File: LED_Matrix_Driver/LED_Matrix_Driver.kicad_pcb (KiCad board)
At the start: 2 copper layers, 64 parts, among them J1 5V_DC, J2 I2C Bus, J3 LED Anode Rows, J4 Columns 24-31 LED Cathodes, J5 Columns 16-23 LED Cathodes, J6 Columns 8-15 LED Cathodes, J7 Columns 0-7 LED Cathodes, U1 ATmega8-16PU, U2 74HC238, U3 MIC2981, U4 HEF4794B, U5 HEF4794B, U6 HEF4794B, U7 HEF4794B, Y1 16MHz

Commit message: Big Commit:
- Hardware files are complete
    - Final hardware iteration until further notice.
- Generated new firmware project with Platform.io in VSCode
    - Will use git more with this
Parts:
- removed C5, C6, C7: 0.1uF, Capacitor_THT:C_Axial_L3.8mm_D2.6mm_P7.50mm_Horizontal
- removed J7: Columns 0-7 LED Cathodes, TerminalBlock_Phoenix:TerminalBlock_Phoenix_MKDS-1,5-8-5.08_1x08_P5.08mm_Horizontal
- removed Y1: 16MHz, Crystal:Crystal_HC49-U_Vertical
- added R43: 200, Resistor_THT:R_Axial_DIN0204_L3.6mm_D1.6mm_P7.62mm_Horizontal, F.Cu at (262.0, 25.4)
- added R44: 200, Resistor_THT:R_Axial_DIN0204_L3.6mm_D1.6mm_P7.62mm_Horizontal, F.Cu at (266.7, 25.4)
- added R45: 200, Resistor_THT:R_Axial_DIN0204_L3.6mm_D1.6mm_P7.62mm_Horizontal, F.Cu at (271.8, 25.4)
- added R46: 200, Resistor_THT:R_Axial_DIN0204_L3.6mm_D1.6mm_P7.62mm_Horizontal, F.Cu at (276.9, 25.4)
- added R47: 200, Resistor_THT:R_Axial_DIN0204_L3.6mm_D1.6mm_P7.62mm_Horizontal, F.Cu at (281.9, 25.4)
- added U8: HEF4794B, Package_DIP:DIP-16_W7.62mm_Socket, F.Cu at (262.9, 47.0)
- C1, C2: value 22pF -> 0.1uF
- C3, C4: moved to F.Cu
- J1: value 5V_DC -> Screw_Terminal_01x02; footprint Connector_BarrelJack:BarrelJack_Horizontal -> TerminalBlock_4Ucon:TerminalBlock_4Ucon_1x02_P3.50mm_Horizontal
- J2: value I2C Bus -> LED Anode Rows; footprint TerminalBlock_Phoenix:TerminalBlock_Phoenix_MKDS-1,5-2-5.08_1x02_P5.08mm_Horizontal -> TerminalBlock_Phoenix:TerminalBlock_Phoenix_MKDS-1,5-8-5.08_1x08_P5.08mm_Horizontal
- J3: value LED Anode Rows -> Columns 24-31 LED Cathodes
- J4: value Columns 24-31 LED Cathodes -> Columns 16-23 LED Cathodes
- J5: value Columns 16-23 LED Cathodes -> Columns 8-15 LED Cathodes
- J6: value Columns 8-15 LED Cathodes -> Columns 0-7 LED Cathodes
- R1, R2: value 10k -> 1M
- R11, R12, R13, R14, R15: value 200 -> 3k3
- R3, R4, R5, R6, R7: value 3k3 -> 1M
- U1: value ATmega8-16PU -> ESP32-DEVKITC-32E; footprint Package_DIP:DIP-28_W7.62mm_Socket -> Arduino:ESP32-DevkitC
- U2: value 74HC238 -> 74HCT244; footprint Package_DIP:DIP-16_W7.62mm_Socket -> Package_DIP:DIP-20_W7.62mm_Socket
- U4: value HEF4794B -> 74HC238
- moved R42 195.4 mm to (256.5, 25.4), turned to 270 degrees
- moved R41 187.5 mm to (251.5, 25.4), turned to 270 degrees
- moved R40 179.8 mm to (246.4, 25.4), turned to 270 degrees
- moved R39 171.5 mm to (240.0, 25.4), turned to 270 degrees
- moved J4 170.7 mm to (162.6, 17.8), turned to 0 degrees
- moved R16 168.8 mm to (120.7, 25.4), turned to 270 degrees
- moved R38 164.5 mm to (234.9, 25.4), turned to 270 degrees
- moved R17 161.9 mm to (125.7, 25.4), turned to 270 degrees
- moved R37 157.7 mm to (229.9, 25.4), turned to 270 degrees
- moved R18 155.3 mm to (130.8, 25.4), turned to 270 degrees
- moved J6 152.2 mm to (246.4, 17.8), turned to 0 degrees
- moved R36 151.4 mm to (224.8, 25.4), turned to 270 degrees
- moved R19 148.4 mm to (135.9, 25.4), turned to 270 degrees
- moved J1 146.1 mm to (121.9, 90.8), turned to 90 degrees
- moved R35 145.5 mm to (219.7, 25.4), turned to 270 degrees
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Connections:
- C1 pad 1: Net-(C1-Pad1) -> +5V
- C2 pad 1: Net-(C2-Pad1) -> +5V
- J1 pad 1: Earth -> +5V
- J1 pad 2: +5V -> Earth
- R1 pad 1: Net-(J2-Pad1) -> Net-(R1-Pad1)
- R1 pad 2: +5V -> Earth
- R11 pad 1: Net-(J4-Pad1) -> Net-(R11-Pad1)
- R12 pad 1: Net-(J4-Pad2) -> Net-(R12-Pad1)
- R13 pad 1: Net-(J4-Pad3) -> Net-(R13-Pad1)
- R14 pad 1: Net-(J4-Pad4) -> Net-(R14-Pad1)
- R15 pad 1: Net-(J4-Pad5) -> Net-(R15-Pad1)
- R16 pad 1: Net-(J4-Pad6) -> Net-(J3-Pad1)
- R17 pad 1: Net-(J4-Pad7) -> Net-(J3-Pad2)
- R18 pad 1: Net-(J4-Pad8) -> Net-(J3-Pad3)
- R19 pad 1: Net-(J5-Pad1) -> Net-(J3-Pad4)
- R2 pad 1: Net-(J2-Pad2) -> Net-(R2-Pad1)
- R2 pad 2: +5V -> Earth
- R20 pad 1: Net-(J5-Pad2) -> Net-(J3-Pad5)
- R21 pad 1: Net-(J5-Pad3) -> Net-(J3-Pad6)
- R22 pad 1: Net-(J5-Pad4) -> Net-(J3-Pad7)
- R23 pad 1: Net-(J5-Pad5) -> Net-(J3-Pad8)
- R24 pad 1: Net-(J5-Pad6) -> Net-(J4-Pad1)
- R25 pad 1: Net-(J5-Pad7) -> Net-(J4-Pad2)
- R26 pad 1: Net-(J5-Pad8) -> Net-(J4-Pad3)
- R27 pad 1: Net-(J6-Pad1) -> Net-(J4-Pad4)
- R28 pad 1: Net-(J6-Pad2) -> Net-(J4-Pad5)
- R29 pad 1: Net-(J6-Pad3) -> Net-(J4-Pad6)
- R3 pad 2: Net-(R3-Pad2) -> Earth
- R30 pad 1: Net-(J6-Pad4) -> Net-(J4-Pad7)
- R31 pad 1: Net-(J6-Pad5) -> Net-(J4-Pad8)
- R32 pad 1: Net-(J6-Pad6) -> Net-(J5-Pad1)
- R33 pad 1: Net-(J6-Pad7) -> Net-(J5-Pad2)
- R34 pad 1: Net-(J6-Pad8) -> Net-(J5-Pad3)
- R35 pad 1: Net-(J7-Pad1) -> Net-(J5-Pad4)
- R36 pad 1: Net-(J7-Pad2) -> Net-(J5-Pad5)
- R37 pad 1: Net-(J7-Pad3) -> Net-(J5-Pad6)
- R38 pad 1: Net-(J7-Pad4) -> Net-(J5-Pad7)
- R39 pad 1: Net-(J7-Pad5) -> Net-(J5-Pad8)
- R4 pad 2: Net-(R4-Pad2) -> Earth
- R40 pad 1: Net-(J7-Pad6) -> Net-(J6-Pad1)
- R41 pad 1: Net-(J7-Pad7) -> Net-(J6-Pad2)
- R42 pad 1: Net-(J7-Pad8) -> Net-(J6-Pad3)
- R5 pad 2: Net-(R5-Pad2) -> Earth
- R6 pad 2: Net-(R6-Pad2) -> Earth
- R7 pad 2: Net-(R7-Pad2) -> Earth
- U1 pad 10: Net-(C2-Pad1) -> Net-(U1-Pad10)
- U1 pad 12: Net-(U1-Pad12) -> Net-(R5-Pad1)
- U1 pad 13: Net-(U1-Pad13) -> Net-(R7-Pad1)
- U1 pad 14: Net-(U1-Pad14) -> Earth
- U1 pad 15: Net-(U1-Pad15) -> Net-(R6-Pad1)
- U1 pad 19: Net-(U1-Pad19) -> +5V
- U1 pad 20: +5V -> Net-(U1-Pad20)
- U1 pad 22: Earth -> Net-(U1-Pad22)
- U1 pad 23: Net-(U1-Pad23) -> Net-(R4-Pad1)
- U1 pad 27: Net-(J2-Pad1) -> Net-(R3-Pad1)
- U1 pad 28: Net-(J2-Pad2) -> Net-(R2-Pad1)
- U1 pad 7: +5V -> Net-(U1-Pad7)
- U1 pad 8: Earth -> Net-(U1-Pad8)
- U1 pad 9: Net-(C1-Pad1) -> Net-(U1-Pad9)
- U2 pad 1: Net-(U1-Pad11) -> Earth
- U2 pad 10: Net-(R5-Pad2) -> Earth
- U2 pad 11: Net-(R6-Pad2) -> Net-(U2-Pad11)
- U2 pad 12: Net-(R7-Pad2) -> Net-(U2-Pad12)
- U2 pad 13: Net-(R8-Pad2) -> Net-(R1-Pad1)
- U2 pad 14: Net-(R9-Pad2) -> Net-(U2-Pad14)
- U2 pad 15: Net-(R10-Pad2) -> Net-(R2-Pad1)
- U2 pad 16: +5V -> Net-(U2-Pad16)
- U2 pad 2: Net-(U1-Pad12) -> Net-(R7-Pad1)
- U2 pad 3: Net-(U1-Pad13) -> Net-(U2-Pad3)
- U2 pad 4: Earth -> Net-(R6-Pad1)
- U2 pad 5: Earth -> Net-(U2-Pad5)
- U2 pad 6: +5V -> Net-(R5-Pad1)
- U2 pad 7: Net-(R3-Pad2) -> Net-(U2-Pad7)
- U2 pad 8: Earth -> Net-(R4-Pad1)
- U2 pad 9: Net-(R4-Pad2) -> Net-(U2-Pad9)
- U3 pad 1: Net-(R10-Pad1) -> Net-(R15-Pad1)
- U3 pad 11: Net-(J3-Pad8) -> Net-(J2-Pad8)
- U3 pad 12: Net-(J3-Pad7) -> Net-(J2-Pad7)
- U3 pad 13: Net-(J3-Pad6) -> Net-(J2-Pad6)
- U3 pad 14: Net-(J3-Pad5) -> Net-(J2-Pad5)
- U3 pad 15: Net-(J3-Pad4) -> Net-(J2-Pad4)
- U3 pad 16: Net-(J3-Pad3) -> Net-(J2-Pad3)
- U3 pad 17: Net-(J3-Pad2) -> Net-(J2-Pad2)
- U3 pad 18: Net-(J3-Pad1) -> Net-(J2-Pad1)
- U3 pad 2: Net-(R9-Pad1) -> Net-(R14-Pad1)
- U3 pad 3: Net-(R8-Pad1) -> Net-(R13-Pad1)
- U3 pad 4: Net-(R7-Pad1) -> Net-(R12-Pad1)
- U3 pad 5: Net-(R6-Pad1) -> Net-(R11-Pad1)
- U3 pad 6: Net-(R5-Pad1) -> Net-(R10-Pad1)
- U3 pad 7: Net-(R4-Pad1) -> Net-(R9-Pad1)
- U3 pad 8: Net-(R3-Pad1) -> Net-(R8-Pad1)
- U4 pad 1: Net-(U1-Pad14) -> Net-(U2-Pad3)
- U4 pad 10: Net-(U4-Pad10) -> Net-(R10-Pad2)
- U4 pad 11: Net-(R18-Pad2) -> Net-(R11-Pad2)
- U4 pad 12: Net-(R17-Pad2) -> Net-(R12-Pad2)
- U4 pad 13: Net-(R16-Pad2) -> Net-(R13-Pad2)
- U4 pad 14: Net-(R15-Pad2) -> Net-(R14-Pad2)
- U4 pad 15: Net-(U1-Pad17) -> Net-(R15-Pad2)
- U4 pad 2: Net-(U1-Pad15) -> Net-(U2-Pad5)
- U4 pad 3: Net-(U1-Pad16) -> Net-(U2-Pad7)
- U4 pad 4: Net-(R11-Pad2) -> Earth
- U4 pad 5: Net-(R12-Pad2) -> Earth
- U4 pad 6: Net-(R13-Pad2) -> +5V
- U4 pad 7: Net-(R14-Pad2) -> Net-(R8-Pad2)
- U4 pad 9: Net-(U4-Pad9) -> Net-(R9-Pad2)
- U5 pad 1: Net-(U1-Pad14) -> Net-(U2-Pad18)
- U5 pad 11: Net-(R26-Pad2) -> Net-(R23-Pad2)
- U5 pad 12: Net-(R25-Pad2) -> Net-(R22-Pad2)
- U5 pad 13: Net-(R24-Pad2) -> Net-(R21-Pad2)
- U5 pad 14: Net-(R23-Pad2) -> Net-(R20-Pad2)
- U5 pad 15: Net-(U1-Pad17) -> Net-(U2-Pad12)
- U5 pad 2: Net-(U4-Pad9) -> Net-(U2-Pad16)
- U5 pad 3: Net-(U1-Pad16) -> Net-(U2-Pad14)
- U5 pad 4: Net-(R19-Pad2) -> Net-(R16-Pad2)
- U5 pad 5: Net-(R20-Pad2) -> Net-(R17-Pad2)
- U5 pad 6: Net-(R21-Pad2) -> Net-(R18-Pad2)
- U5 pad 7: Net-(R22-Pad2) -> Net-(R19-Pad2)
- U6 pad 1: Net-(U1-Pad14) -> Net-(U2-Pad18)
- U6 pad 11: Net-(R34-Pad2) -> Net-(R31-Pad2)
- U6 pad 12: Net-(R33-Pad2) -> Net-(R30-Pad2)
- U6 pad 13: Net-(R32-Pad2) -> Net-(R29-Pad2)
- U6 pad 14: Net-(R31-Pad2) -> Net-(R28-Pad2)
- U6 pad 15: Net-(U1-Pad17) -> Net-(U2-Pad12)
- U6 pad 3: Net-(U1-Pad16) -> Net-(U2-Pad14)
- U6 pad 4: Net-(R27-Pad2) -> Net-(R24-Pad2)
- U6 pad 5: Net-(R28-Pad2) -> Net-(R25-Pad2)
- U6 pad 6: Net-(R29-Pad2) -> Net-(R26-Pad2)
- U6 pad 7: Net-(R30-Pad2) -> Net-(R27-Pad2)
- U7 pad 1: Net-(U1-Pad14) -> Net-(U2-Pad18)
- U7 pad 11: Net-(R42-Pad2) -> Net-(R39-Pad2)
- U7 pad 12: Net-(R41-Pad2) -> Net-(R38-Pad2)
- U7 pad 13: Net-(R40-Pad2) -> Net-(R37-Pad2)
- U7 pad 14: Net-(R39-Pad2) -> Net-(R36-Pad2)
- U7 pad 15: Net-(U1-Pad17) -> Net-(U2-Pad12)
- U7 pad 3: Net-(U1-Pad16) -> Net-(U2-Pad14)
- U7 pad 4: Net-(R35-Pad2) -> Net-(R32-Pad2)
- U7 pad 5: Net-(R36-Pad2) -> Net-(R33-Pad2)
- U7 pad 6: Net-(R37-Pad2) -> Net-(R34-Pad2)
- U7 pad 7: Net-(R38-Pad2) -> Net-(R35-Pad2)
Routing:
- net Net-(U1-Pad17): track 163.9 -> 0.00 mm
- net Net-(U1-Pad14): track 161.5 -> 0.00 mm
- net Net-(U2-Pad18): track 0.00 -> 159.6 mm, vias 0 -> 1
- net Net-(U2-Pad12): track 0.00 -> 158.8 mm, vias 0 -> 1
- net Net-(U1-Pad16): track 153.0 -> 0.00 mm, vias 4 -> 0
- net Net-(U2-Pad14): track 0.00 -> 147.0 mm, vias 0 -> 3
- net Net-(R1-Pad1): track 0.00 -> 80.8 mm
- net Net-(U2-Pad16): track 0.00 -> 76.2 mm, vias 0 -> 1
- net Net-(R2-Pad1): track 0.00 -> 70.3 mm
- net Net-(J2-Pad2): track 75.3 -> 9.42 mm
- net Net-(J2-Pad1): track 74.9 -> 9.42 mm
- net Net-(R5-Pad1): track 7.62 -> 66.3 mm
- net Net-(R4-Pad1): track 7.62 -> 63.4 mm
- net Net-(R3-Pad1): track 7.62 -> 62.3 mm
- net Net-(U1-Pad15): track 51.8 -> 0.00 mm, vias 1 -> 0
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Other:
- board outline added: 168.3 x 82.6 mm
- board text added: "5V"
- board text added: "8x32 LED Matrix Driver"
- board text added: "BACK OF BOARD"
- board text added: "Copyright (C) Matt Bowen 2023"
- board text added: "Designed by Matt Bowen"

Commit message: Made some minor tweaks to the PCB layout. Will not physically implement them until later date.
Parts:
- removed C1: 0.1uF, Capacitor_THT:C_Axial_L3.8mm_D2.6mm_P7.50mm_Horizontal
- moved U1 58.4 mm to (179.7, 68.6), turned to 270 degrees
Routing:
- net Net-(R6-Pad1): track 51.5 -> 74.1 mm
- net Net-(R4-Pad1): track 63.4 -> 81.8 mm
- net Net-(R1-Pad1): track 80.8 -> 65.9 mm
- net Net-(R7-Pad1): track 51.5 -> 60.8 mm
- net Net-(R2-Pad1): track 70.3 -> 65.9 mm
- net Net-(R3-Pad1): track 62.3 -> 65.2 mm
- net Net-(R5-Pad1): track 66.3 -> 68.4 mm
- net +5V: track 476.7 -> 475.1 mm
- net Earth: vias 20 -> 37

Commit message: Created a new PCB layout for LEDMatrixDriver board
- More compact
- Removed unused capacitors
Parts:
- removed C2, C3, C4: 0.1uF, Capacitor_THT:C_Axial_L3.8mm_D2.6mm_P7.50mm_Horizontal
- R1, R2, R3, R4, R5, R6, R7: footprint Resistor_THT:R_Axial_DIN0204_L3.6mm_D1.6mm_P7.62mm_Horizontal -> Resistor_THT:R_Axial_DIN0207_L6.3mm_D2.5mm_P10.16mm_Horizontal; moved to B.Cu
- R10, R11, R12, R13, R14, R15, R16, R17, R18, R19, R20, R21, R22, R23, R24, R25, R26, R27, R28, R29, R30, R31, R32, R33, R34, R35, R36, R37, R38, R39, R40, R41, R42, R43, R44, R45, R46, R47, R8, R9: footprint Resistor_THT:R_Axial_DIN0204_L3.6mm_D1.6mm_P7.62mm_Horizontal -> Resistor_THT:R_Axial_DIN0207_L6.3mm_D2.5mm_P10.16mm_Horizontal
- moved R4 191.5 mm to (23.5, 63.5), turned to 90 degrees
- moved R1 187.3 mm to (27.3, 63.5)
- moved R6 186.0 mm to (19.7, 53.3)
- moved R2 174.6 mm to (34.9, 63.5)
- moved R3 173.4 mm to (31.1, 63.5)
- moved R5 172.2 mm to (38.7, 53.3)
- moved R7 158.3 mm to (42.5, 53.3)
- moved U2 134.5 mm to (64.8, 47.0), turned to 0 degrees
- moved U8 127.6 mm to (135.3, 48.9), turned to 0 degrees
- moved U1 118.7 mm to (61.6, 57.1)
- moved R43 105.8 mm to (156.2, 24.1)
- moved R42 105.4 mm to (151.1, 24.1)
- moved R46 105.4 mm to (171.4, 24.1)
- moved R16 105.4 mm to (15.2, 24.1)
- moved R21 105.4 mm to (40.6, 24.1)
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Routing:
- net +5V: track 475.1 -> 233.9 mm, vias 3 -> 0
- net Net-(U2-Pad5): track 33.1 -> 129.4 mm, vias 0 -> 2
- net Net-(U2-Pad18): track 159.6 -> 67.8 mm, vias 1 -> 0
- net Net-(U2-Pad7): track 25.8 -> 113.7 mm
- net Net-(U2-Pad3): track 40.3 -> 126.8 mm, vias 0 -> 1
- net Net-(U2-Pad14): track 147.0 -> 73.1 mm, vias 3 -> 0
- net Net-(U2-Pad12): track 158.8 -> 94.4 mm
- net Net-(U2-Pad16): track 76.2 -> 12.3 mm, vias 1 -> 0
- net Net-(R20-Pad2): track 6.88 -> 67.7 mm, vias 0 -> 1
- net Net-(R21-Pad2): track 6.88 -> 65.2 mm, vias 0 -> 2
- net Net-(R22-Pad2): track 7.93 -> 62.6 mm, vias 0 -> 1
- net Net-(R16-Pad2): track 29.9 -> 82.9 mm, vias 0 -> 1
- net Net-(R17-Pad2): track 27.4 -> 80.4 mm, vias 0 -> 2
- net Net-(R23-Pad2): track 8.98 -> 60.1 mm, vias 0 -> 2
- net Net-(R18-Pad2): track 27.1 -> 77.9 mm, vias 0 -> 1
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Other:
- board size 168.3 x 82.6 mm -> 200 x 66 mm
- board text removed: "5V"
- board text removed: "8x32 LED Matrix Driver"
- board text removed: "BACK OF BOARD"
- board text removed: "Copyright (C) Matt Bowen 2023"
- board text removed: "Designed by Matt Bowen"

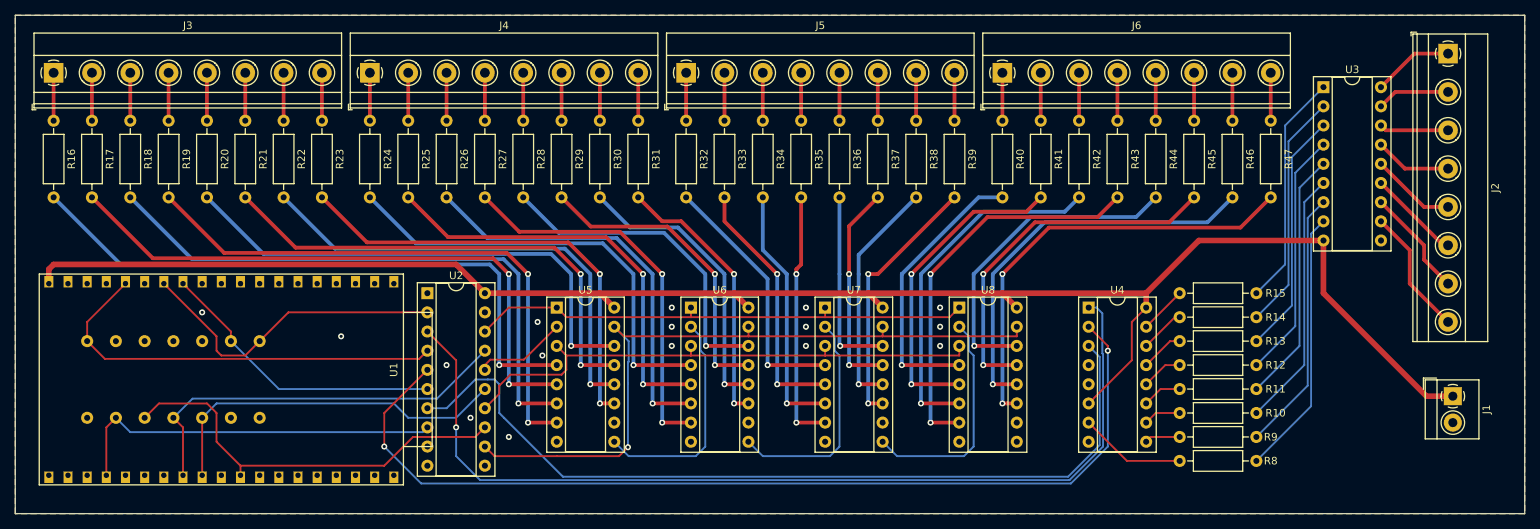
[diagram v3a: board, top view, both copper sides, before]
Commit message: Modified design to include decoupling capacitors. PCB is now 4 layers with power and ground planes
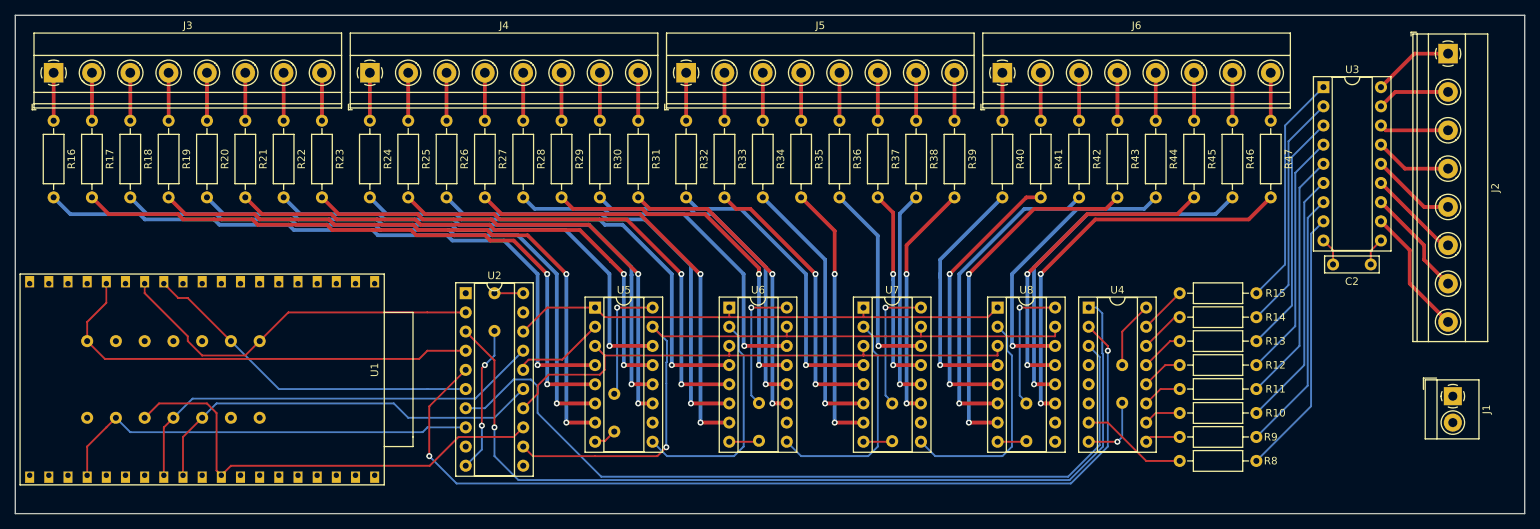
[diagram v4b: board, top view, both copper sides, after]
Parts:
- added C1: 0.1uF, Capacitor_THT:C_Rect_L7.0mm_W2.0mm_P5.00mm, B.Cu at (73.7, 52.0)
- added C2: 0.1uF, Capacitor_THT:C_Rect_L7.0mm_W2.0mm_P5.00mm, F.Cu at (189.8, 43.2)
- added C3: 0.1uF, Capacitor_THT:C_Rect_L7.0mm_W2.0mm_P5.00mm, B.Cu at (156.8, 56.5)
- added C4: 0.1uF, Capacitor_THT:C_Rect_L7.0mm_W2.0mm_P5.00mm, B.Cu at (89.5, 60.3)
- added C5: 0.1uF, Capacitor_THT:C_Rect_L7.0mm_W2.0mm_P5.00mm, B.Cu at (108.7, 61.5)
- added C6: 0.1uF, Capacitor_THT:C_Rect_L7.0mm_W2.0mm_P5.00mm, B.Cu at (126.4, 61.6)
- added C7: 0.1uF, Capacitor_THT:C_Rect_L7.0mm_W2.0mm_P5.00mm, B.Cu at (144.1, 61.6)
- moved U6 5.08 mm to (104.8, 48.9)
- moved U7 5.08 mm to (122.6, 48.9)
- moved U8 5.08 mm to (140.3, 48.9)
- moved U2 5.08 mm to (69.8, 47.0)
- moved U5 5.08 mm to (87.0, 48.9)
- moved U1 2.54 mm to (59.1, 57.1)
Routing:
- net +5V: track 233.9 -> 85.3 mm, vias 0 -> 4
- net Earth: track 0.00 -> 47.1 mm, vias 16 -> 3
- net Net-(R7-Pad1): track 42.4 -> 50.0 mm
- net Net-(R1-Pad1): track 54.9 -> 62.0 mm
- net Net-(R5-Pad1): track 38.9 -> 45.8 mm
- net Net-(R45-Pad2): track 48.7 -> 42.1 mm
- net Net-(R4-Pad1): track 50.5 -> 56.6 mm
- net Net-(R2-Pad1): track 48.2 -> 54.4 mm
- net Net-(R26-Pad2): track 53.7 -> 59.5 mm
- net Net-(R30-Pad2): track 38.5 -> 44.1 mm
- net Net-(R22-Pad2): track 62.6 -> 68.2 mm
- net Net-(U2-Pad5): track 129.4 -> 123.8 mm
- net Net-(R29-Pad2): track 41.0 -> 46.6 mm
- net Net-(R32-Pad2): track 34.3 -> 39.8 mm
- net Net-(R46-Pad2): track 53.7 -> 48.4 mm
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- added copper zone on In1.Cu, net +5V
- added copper zone on In2.Cu, net Earth
- removed copper zone on B.Cu, net Earth
- removed copper zone on F.Cu, net Earth
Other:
- copper layers 2 -> 4

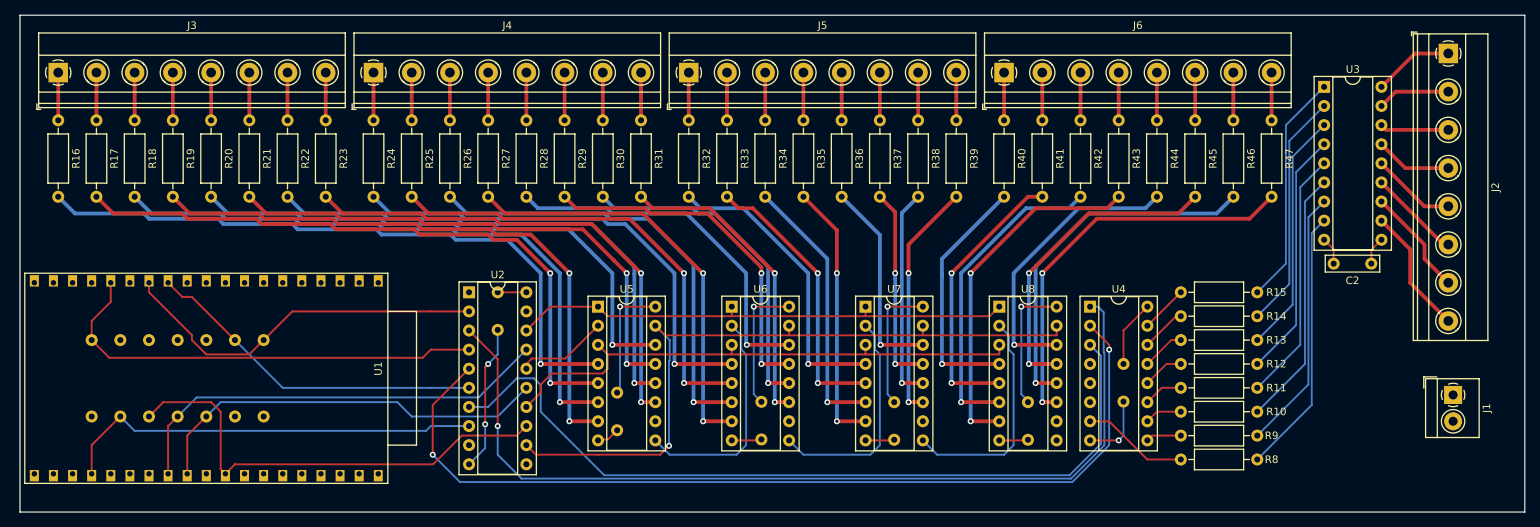
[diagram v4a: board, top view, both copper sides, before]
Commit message: Added 6 push buttons to the PCB as well as 4 mounting holes
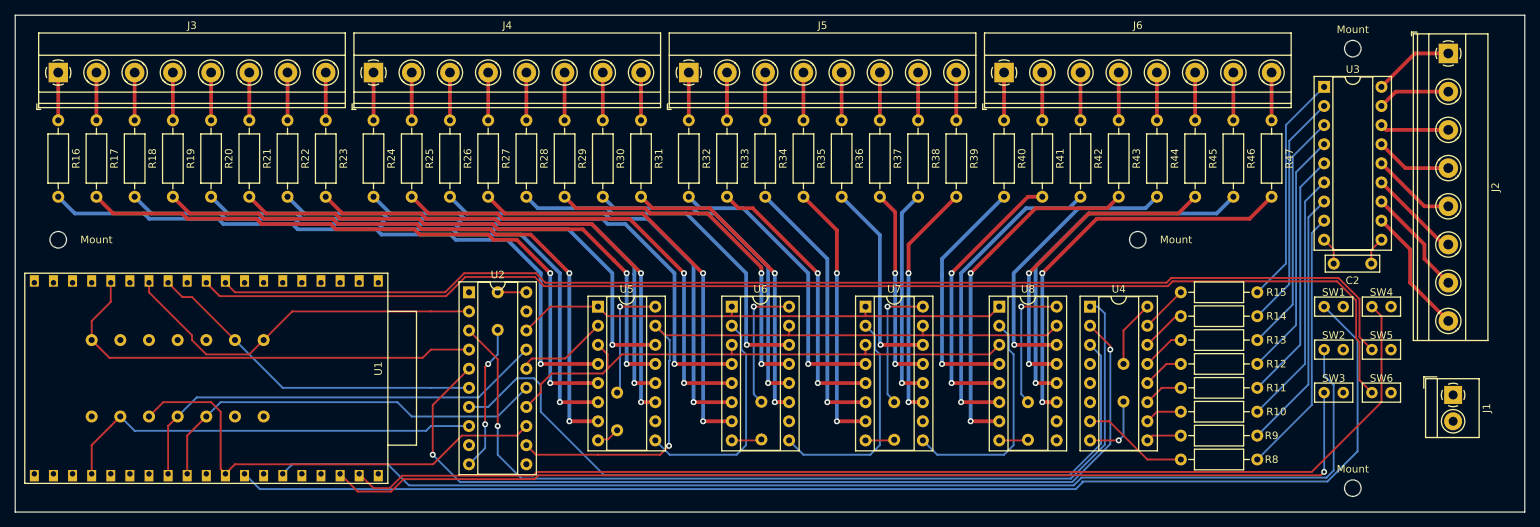
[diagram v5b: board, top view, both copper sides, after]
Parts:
- added Mount: MountingHole_2.2mm_M2, MountingHole:MountingHole_2.2mm_M2, F.Cu at (187.3, 73.0)
- added Mount: MountingHole_2.2mm_M2, MountingHole:MountingHole_2.2mm_M2, F.Cu at (187.3, 14.6)
- added Mount: MountingHole_2.2mm_M2, MountingHole:MountingHole_2.2mm_M2, F.Cu at (158.8, 40.0)
- added Mount: MountingHole_2.2mm_M2, MountingHole:MountingHole_2.2mm_M2, F.Cu at (15.2, 40.0)
- added SW1: OK, Arduino:Custom_Pin_Header, F.Cu at (184.8, 47.0)
- added SW2: BACK, Arduino:Custom_Pin_Header, F.Cu at (184.8, 52.7)
- added SW3: UP, Arduino:Custom_Pin_Header, F.Cu at (184.8, 58.4)
- added SW4: DOWN, Arduino:Custom_Pin_Header, F.Cu at (191.1, 47.0)
- added SW5: LEFT, Arduino:Custom_Pin_Header, F.Cu at (191.1, 52.7)
- added SW6: RIGHT, Arduino:Custom_Pin_Header, F.Cu at (191.1, 58.4)
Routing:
- net Net-(SW1-Pad1): track 0.00 -> 172.0 mm
- net Net-(SW6-Pad1): track 0.00 -> 169.6 mm
- net Net-(SW5-Pad1): track 0.00 -> 161.7 mm
- net Net-(SW2-Pad1): track 0.00 -> 158.8 mm
- net Net-(SW4-Pad1): track 0.00 -> 154.6 mm
- net Net-(SW3-Pad1): track 0.00 -> 143.4 mm, vias 0 -> 1
- net Net-(U2-Pad12): track 94.4 -> 93.7 mm
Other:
- board size 200 x 66 mm -> 200.7 x 66 mm

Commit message: Updated the PCB. Now includes solder points for a few buttons
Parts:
- removed Mount (x4): MountingHole_2.2mm_M2, MountingHole:MountingHole_2.2mm_M2
- F1: renamed from SW3; value UP -> F1
- F2: renamed from SW4; value DOWN -> F2
- F3: renamed from SW5; value LEFT -> F3
- F4: renamed from SW6; value RIGHT -> F4
- renumbered SW2 to Back, SW1 to Ok

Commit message: Updated Driver board to include sinlge header for all 6 buttons
Created new daughter board to hold the buttons
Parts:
- removed Back: BACK, Arduino:Custom_Pin_Header
- removed F1: F1, Arduino:Custom_Pin_Header
- removed F2: F2, Arduino:Custom_Pin_Header
- removed F3: F3, Arduino:Custom_Pin_Header
- removed F4: F4, Arduino:Custom_Pin_Header
- removed Ok: OK, Arduino:Custom_Pin_Header
- added J7: Buttons, Arduino:Custom_Pin_Header, F.Cu at (186.7, 64.8)
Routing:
- net Net-(J7-Pad1): track 172.0 -> 152.5 mm
- net Net-(J7-Pad6): track 169.6 -> 156.9 mm
- net Net-(J7-Pad4): track 154.6 -> 142.4 mm
- net Net-(J7-Pad2): track 158.8 -> 149.0 mm
- net Net-(J7-Pad5): track 161.7 -> 159.2 mm
- net Net-(J7-Pad3): vias 1 -> 0

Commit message: Added some text to the boards
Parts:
- added  : , MountingHole:MountingHole_2.2mm_M2, F.Cu at (17.8, 40.6)
- added  : , MountingHole:MountingHole_2.2mm_M2, F.Cu at (172.7, 40.6)
- added  : , MountingHole:MountingHole_2.2mm_M2, F.Cu at (187.3, 71.8)
- added  : , MountingHole:MountingHole_2.2mm_M2, F.Cu at (187.3, 14.0)
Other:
- board text added: "5V"
- board text added: "Back of Board"
- board text added: "Copyright (C) Matt Bowen 2023"
- board text added: "Designed by Matt Bowen"
- board text added: "GND"
- board text added: "LED Matrix Driver V1.1"
